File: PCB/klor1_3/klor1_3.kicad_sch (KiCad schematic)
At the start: 88 parts, among them J1 MJ-4PP-9, J2 Haptic Buzz, J3 lv27, SW1 SW_PUSH-MX_W_LED, SW10 SW_PUSH-MX_W_LED, SW11 SW_PUSH-MX_W_LED, SW12 SW_PUSH-MX_W_LED, SW13 SW_PUSH-MX_W_LED, SW14 SW_PUSH-MX_W_LED, SW15 SW_PUSH-MX_W_LED, SW16 SW_PUSH-MX_W_LED, SW17 SW_PUSH-MX_W_LED, SW18 RotaryEncoder_Switch, SW19 SW_PUSH-MX_W_LED, SW2 SW_PUSH-MX_W_LED, SW20 SW_PUSH-MX_W_LED, SW21 SW_PUSH-MX_W_LED, SW22 SW_PUSH-MX_W_LED, SW3 SW_PUSH-MX_W_LED, SW4 SW_PUSH-MX_W_LED, SW5 SW_PUSH-MX_W_LED, SW6 SW_PUSH-MX_W_LED, SW7 SW_PUSH-MX_W_LED, SW8 SW_PUSH-MX_W_LED, SW9 SW_PUSH-MX_W_LED, U1 ProMicro

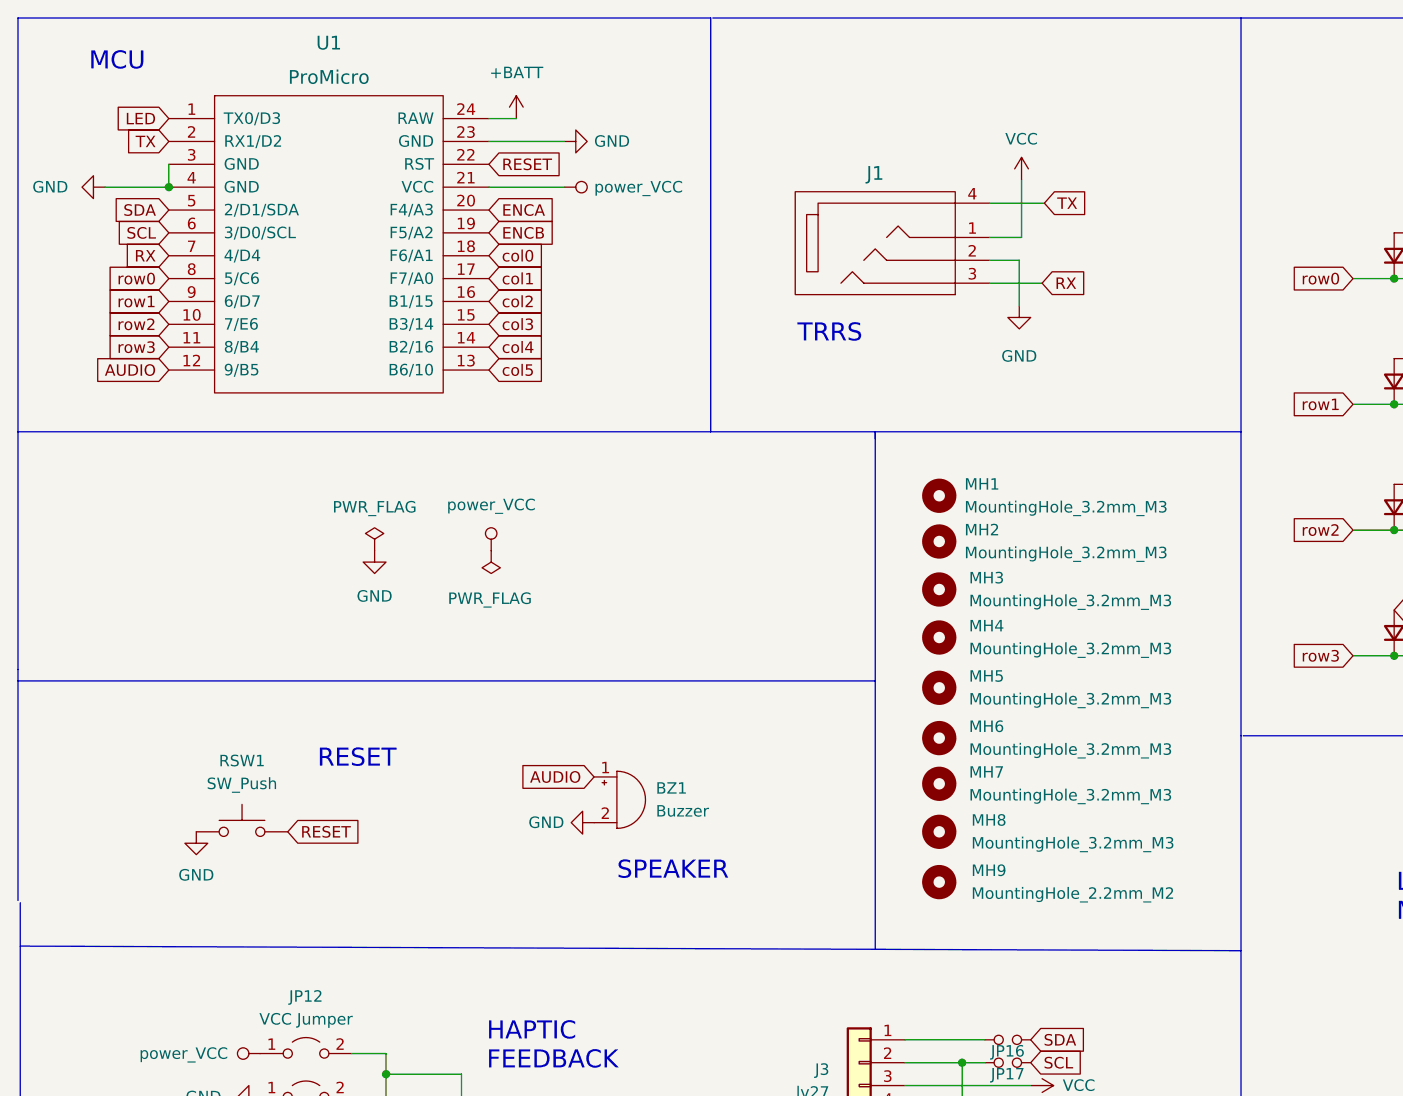
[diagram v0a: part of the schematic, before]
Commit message: adding connector for cirque
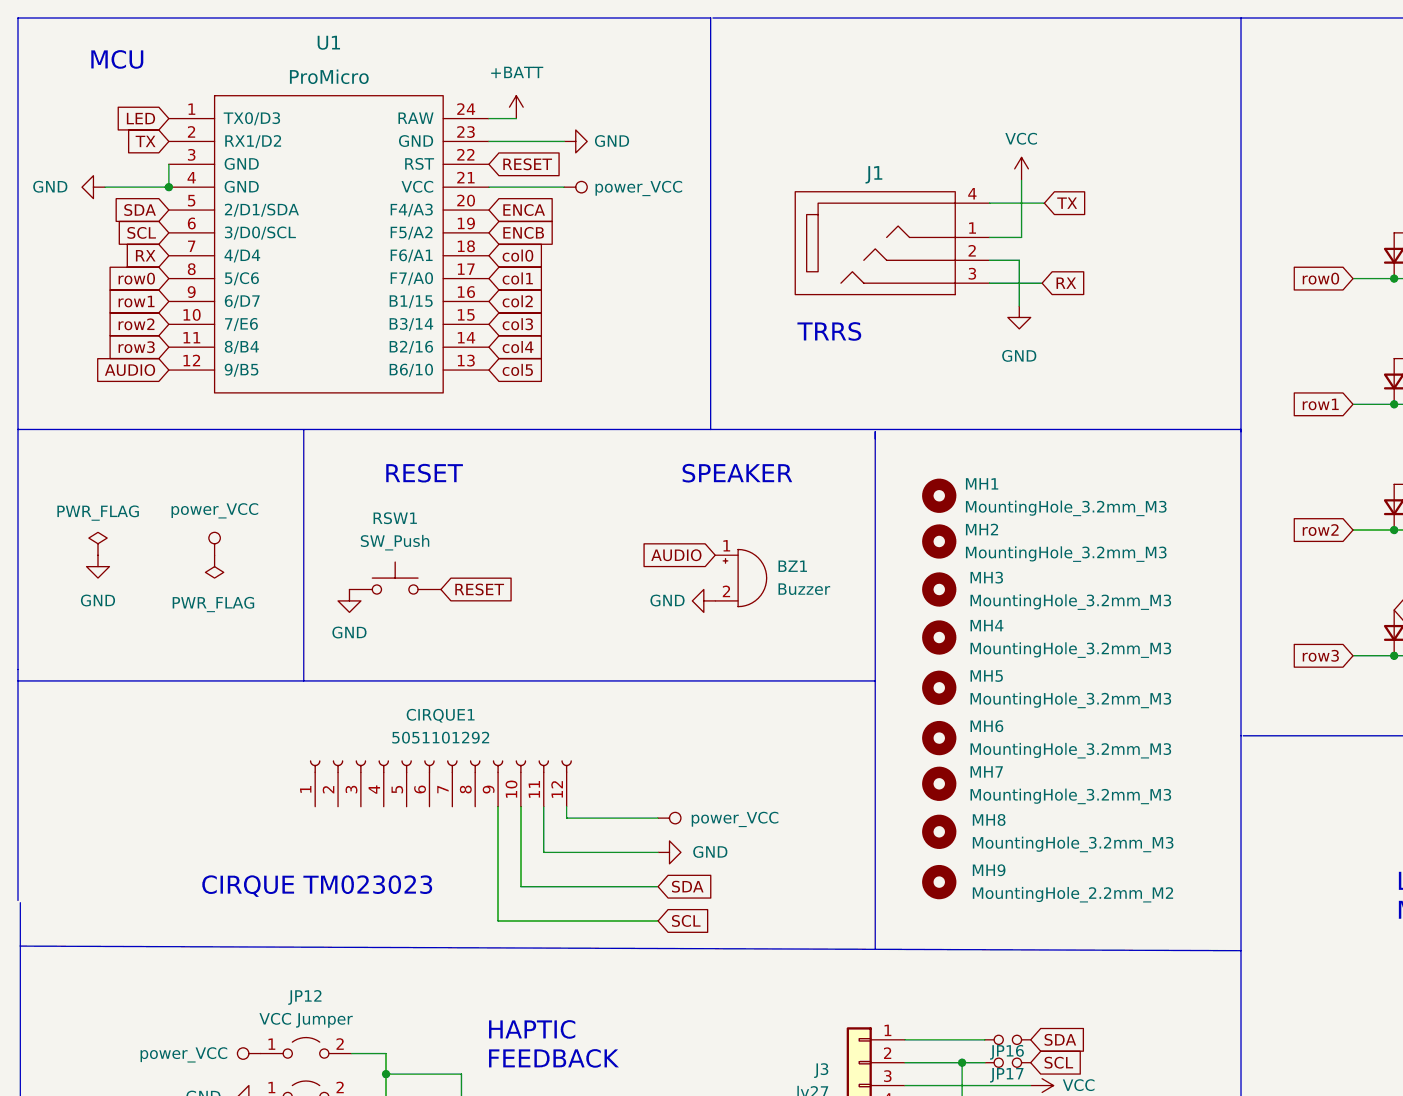
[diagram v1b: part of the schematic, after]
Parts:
- added CIRQUE1: 5051101292, KLOR:Molex_505110-1292_1x12-1SH_P0.5mm Molex 0.50mm Pitch Easy-On Type FFC Connector, symbol Connector:Conn_01x12_Female
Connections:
- net GND: now also CIRQUE1.11 (Pin_11)
- net SCL: now also CIRQUE1.9 (Pin_9)
- net SDA: now also CIRQUE1.10 (Pin_10)
- net VCC: now also CIRQUE1.12 (Pin_12)
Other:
- note added: "CIRQUE TM023023"
- moved on the sheet: BZ1, RSW1
